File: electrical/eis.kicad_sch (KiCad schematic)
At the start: 51 parts

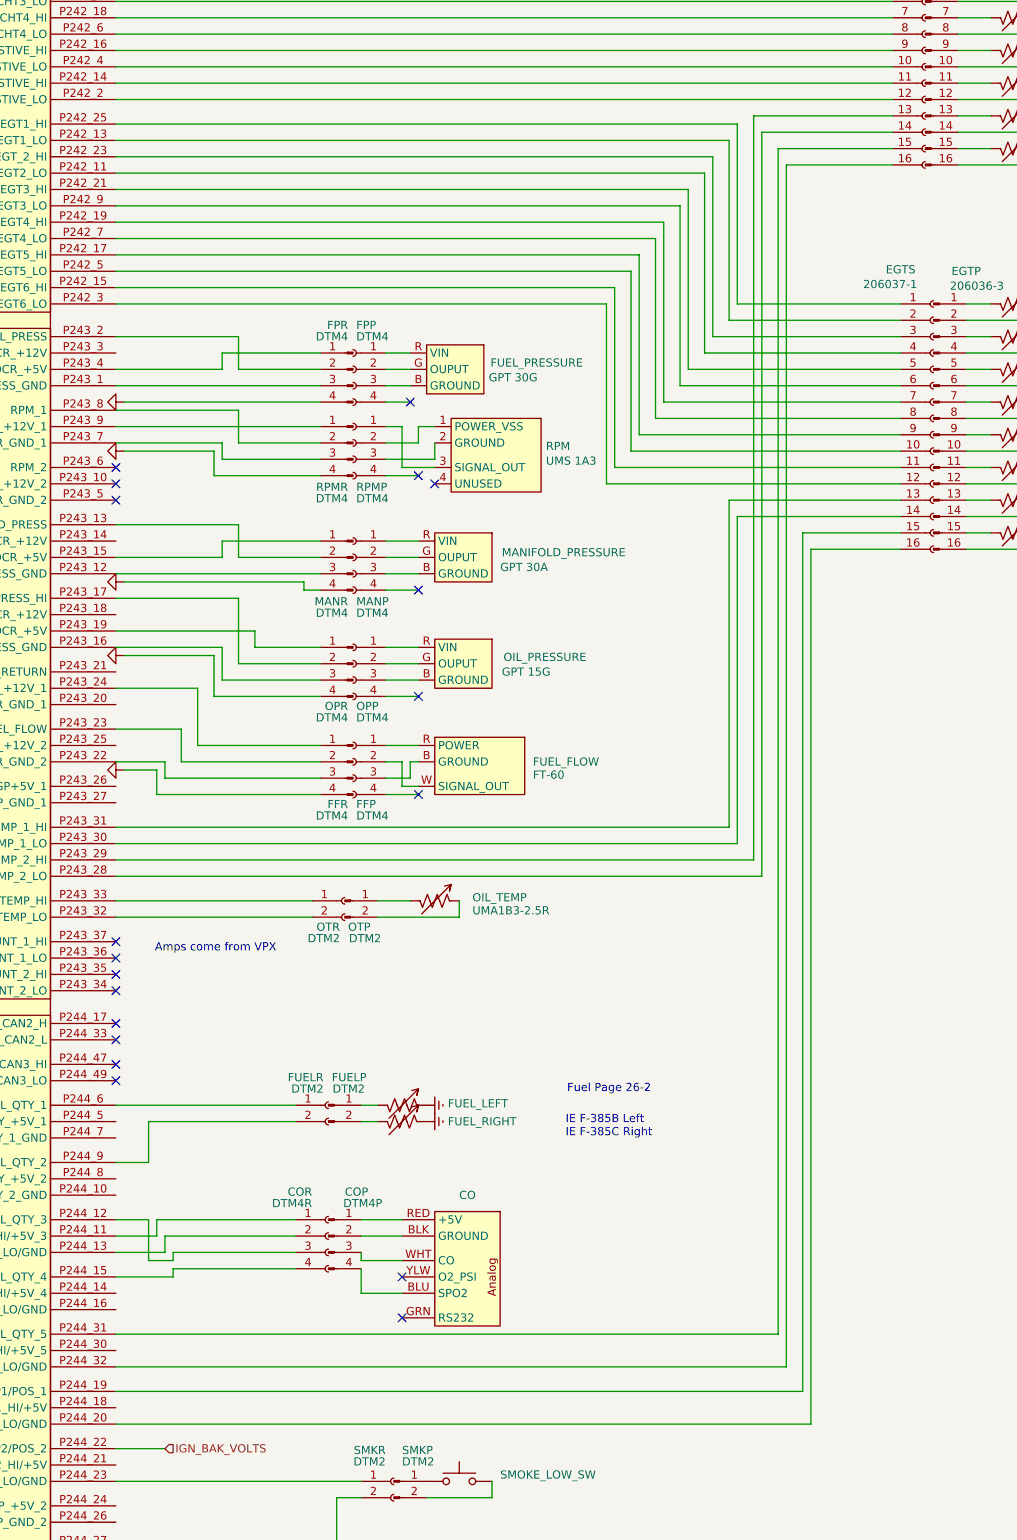
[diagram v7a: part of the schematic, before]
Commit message: Moved extra air temp sensors to the same GEA connector from the CHT or EGT respectively
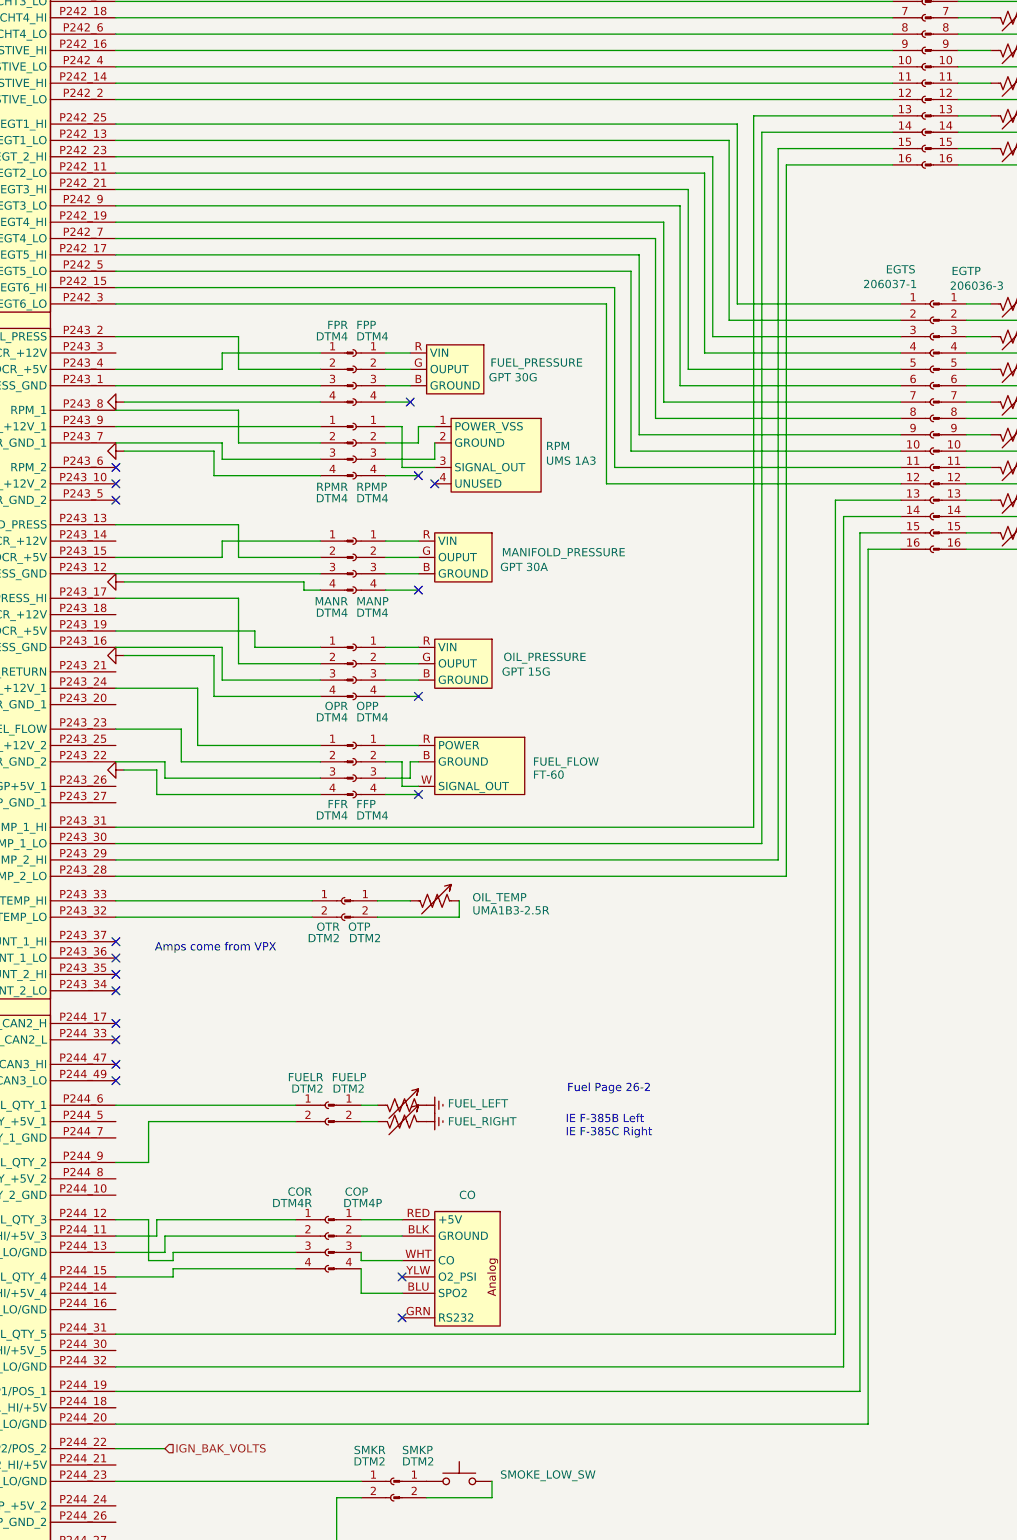
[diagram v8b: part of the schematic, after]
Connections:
- net at CHTS.13 (Pin_13): now also GEA24.P243_31 (POS_6/TIT_1/MISC_TEMP_1_HI); no longer GEA24.P243_29 (POS_7/TIT_2/MISC_TEMP_2_HI)
- net at CHTS.14 (Pin_14): now also GEA24.P243_30 (POS_6/TIT_1/MISC_TEMP_1_LO); no longer GEA24.P243_28 (POS_7/TIT_2/MISC_TEMP_2_LO)
- net at CHTS.15 (Pin_15): now also GEA24.P243_29 (POS_7/TIT_2/MISC_TEMP_2_HI); no longer GEA24.P244_31 (POS_5/GP_5/FUEL_QTY_5)
- net at CHTS.16 (Pin_16): now also GEA24.P243_28 (POS_7/TIT_2/MISC_TEMP_2_LO); no longer GEA24.P244_32 (POS_5_LO/GND)
- net at EGTS.13 (Pin_13): now also GEA24.P244_31 (POS_5/GP_5/FUEL_QTY_5); no longer GEA24.P243_31 (POS_6/TIT_1/MISC_TEMP_1_HI)
- net at EGTS.14 (Pin_14): now also GEA24.P244_32 (POS_5_LO/GND); no longer GEA24.P243_30 (POS_6/TIT_1/MISC_TEMP_1_LO)
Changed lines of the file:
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@@
 	(title_block
 		(title "EIS")
-		(date "2025-10-15")
-		(rev "1.1.14")
+		(date "2025-10-22")
+		(rev "1.1.18")
 		(company "N78HR")
 	)
@@
 	(wire
 		(pts
-			(xy 67.31 280.67) (xy 175.26 280.67)
+			(xy 166.37 187.96) (xy 166.37 77.47)
+		)
+		(stroke
+			(width 0)
+			(type default)
+		)
+	)
+	(wire
+		(pts
+			(xy 67.31 280.67) (xy 184.15 280.67)
 		)
 		(stroke
@@
 	(wire
 		(pts
-			(xy 67.31 190.5) (xy 163.83 190.5)
-		)
-		(stroke
-			(width 0)
-			(type default)
-		)
-	)
-	(wire
-		(pts
 			(xy 83.82 114.3) (xy 99.06 114.3)
 		)
@@
 	(wire
 		(pts
-			(xy 167.64 195.58) (xy 167.64 80.01)
-		)
-		(stroke
-			(width 0)
-			(type default)
-		)
-	)
-	(wire
-		(pts
 			(xy 99.06 160.02) (xy 88.9 160.02)
 		)
@@
 	(wire
 		(pts
+			(xy 170.18 193.04) (xy 170.18 82.55)
+		)
+		(stroke
+			(width 0)
+			(type default)
+		)
+	)
+	(wire
+		(pts
 			(xy 67.31 123.19) (xy 86.36 123.19)
 		)
@@
 	(wire
 		(pts
-			(xy 67.31 187.96) (xy 162.56 187.96)
-		)
-		(stroke
-			(width 0)
-			(type default)
-		)
-	)
-	(wire
-		(pts
 			(xy 198.12 57.15) (xy 203.2 57.15)
 		)
@@
 	(wire
 		(pts
-			(xy 173.99 275.59) (xy 173.99 142.24)
-		)
-		(stroke
-			(width 0)
-			(type default)
-		)
-	)
-	(wire
-		(pts
-			(xy 67.31 275.59) (xy 173.99 275.59)
+			(xy 182.88 275.59) (xy 182.88 142.24)
+		)
+		(stroke
+			(width 0)
+			(type default)
+		)
+	)
+	(wire
+		(pts
+			(xy 67.31 275.59) (xy 182.88 275.59)
 		)
 		(stroke
@@
 	(wire
 		(pts
-			(xy 163.83 190.5) (xy 163.83 139.7)
+			(xy 180.34 139.7) (xy 180.34 271.78)
 		)
 		(stroke
@@
 	(wire
 		(pts
-			(xy 170.18 266.7) (xy 170.18 82.55)
-		)
-		(stroke
-			(width 0)
-			(type default)
-		)
-	)
-	(wire
-		(pts
-			(xy 171.45 271.78) (xy 171.45 85.09)
-		)
-		(stroke
-			(width 0)
-			(type default)
-		)
-	)
-	(wire
-		(pts
 			(xy 67.31 24.13) (xy 78.74 24.13)
 		)
@@
 	(wire
 		(pts
-			(xy 67.31 266.7) (xy 170.18 266.7)
-		)
-		(stroke
-			(width 0)
-			(type default)
-		)
-	)
-	(wire
-		(pts
 			(xy 109.22 175.26) (xy 114.3 175.26)
 		)
@@
 	(wire
 		(pts
+			(xy 67.31 195.58) (xy 171.45 195.58)
+		)
+		(stroke
+			(width 0)
+			(type default)
+		)
+	)
+	(wire
+		(pts
 			(xy 83.82 116.84) (xy 83.82 114.3)
 		)
@@
 	(wire
 		(pts
-			(xy 173.99 142.24) (xy 189.23 142.24)
+			(xy 182.88 142.24) (xy 189.23 142.24)
+		)
+		(stroke
+			(width 0)
+			(type default)
+		)
+	)
+	(wire
+		(pts
+			(xy 67.31 187.96) (xy 166.37 187.96)
 		)
 		(stroke
@@
 	(wire
 		(pts
+			(xy 167.64 190.5) (xy 167.64 80.01)
+		)
+		(stroke
+			(width 0)
+			(type default)
+		)
+	)
+	(wire
+		(pts
 			(xy 210.82 74.93) (xy 210.82 72.39)
 		)
@@
 	(wire
 		(pts
-			(xy 166.37 193.04) (xy 166.37 77.47)
-		)
-		(stroke
-			(width 0)
-			(type default)
-		)
-	)
-	(wire
-		(pts
 			(xy 86.36 116.84) (xy 99.06 116.84)
 		)
@@
 	(wire
 		(pts
+			(xy 67.31 266.7) (xy 179.07 266.7)
+		)
+		(stroke
+			(width 0)
+			(type default)
+		)
+	)
+	(wire
+		(pts
 			(xy 67.31 125.73) (xy 99.06 125.73)
 		)
@@
 	(wire
 		(pts
+			(xy 67.31 190.5) (xy 167.64 190.5)
+		)
+		(stroke
+			(width 0)
+			(type default)
+		)
+	)
+	(wire
+		(pts
 			(xy 109.22 114.3) (xy 113.03 114.3)
 		)
@@
 	(wire
 		(pts
+			(xy 171.45 195.58) (xy 171.45 85.09)
+		)
+		(stroke
+			(width 0)
+			(type default)
+		)
+	)
+	(wire
+		(pts
 			(xy 109.22 160.02) (xy 114.3 160.02)
 		)
@@
 	(wire
 		(pts
-			(xy 67.31 193.04) (xy 166.37 193.04)
-		)
-		(stroke
-			(width 0)
-			(type default)
-		)
-	)
-	(wire
-		(pts
 			(xy 99.06 167.64) (xy 82.55 167.64)
 		)
@@
 	(wire
 		(pts
-			(xy 67.31 271.78) (xy 171.45 271.78)
+			(xy 67.31 271.78) (xy 180.34 271.78)
 		)
 		(stroke
@@
 	(wire
 		(pts
-			(xy 162.56 137.16) (xy 189.23 137.16)
+			(xy 179.07 137.16) (xy 189.23 137.16)
 		)
 		(stroke
@@
 	(wire
 		(pts
-			(xy 175.26 280.67) (xy 175.26 144.78)
+			(xy 184.15 280.67) (xy 184.15 144.78)
 		)
 		(stroke
@@
 	(wire
 		(pts
+			(xy 67.31 193.04) (xy 170.18 193.04)
+		)
+		(stroke
+			(width 0)
+			(type default)
+		)
+	)
+	(wire
+		(pts
 			(xy 96.52 38.1) (xy 96.52 30.48)
 		)
@@
 	(wire
 		(pts
-			(xy 175.26 144.78) (xy 189.23 144.78)
+			(xy 184.15 144.78) (xy 189.23 144.78)
 		)
 		(stroke
@@
 	(wire
 		(pts
-			(xy 67.31 195.58) (xy 167.64 195.58)
-		)
-		(stroke
-			(width 0)
-			(type default)
-		)
-	)
-	(wire
-		(pts
 			(xy 198.12 80.01) (xy 210.82 80.01)
 		)
@@
 	(wire
 		(pts
-			(xy 163.83 139.7) (xy 189.23 139.7)
-		)
-		(stroke
-			(width 0)
-			(type default)
-		)
-	)
-	(wire
-		(pts
-			(xy 162.56 187.96) (xy 162.56 137.16)
-		)
-		(stroke
+			(xy 180.34 139.7) (xy 189.23 139.7)
+		)
+		(stroke
+			(width 0)
+			(type default)
+		)
+	)
+	(wire
+		(pts
+			(xy 179.07 137.16) (xy 179.07 266.7)
+		)
+		(stroke
